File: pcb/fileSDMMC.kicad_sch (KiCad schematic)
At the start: 6 parts, among them J4 MicroSd

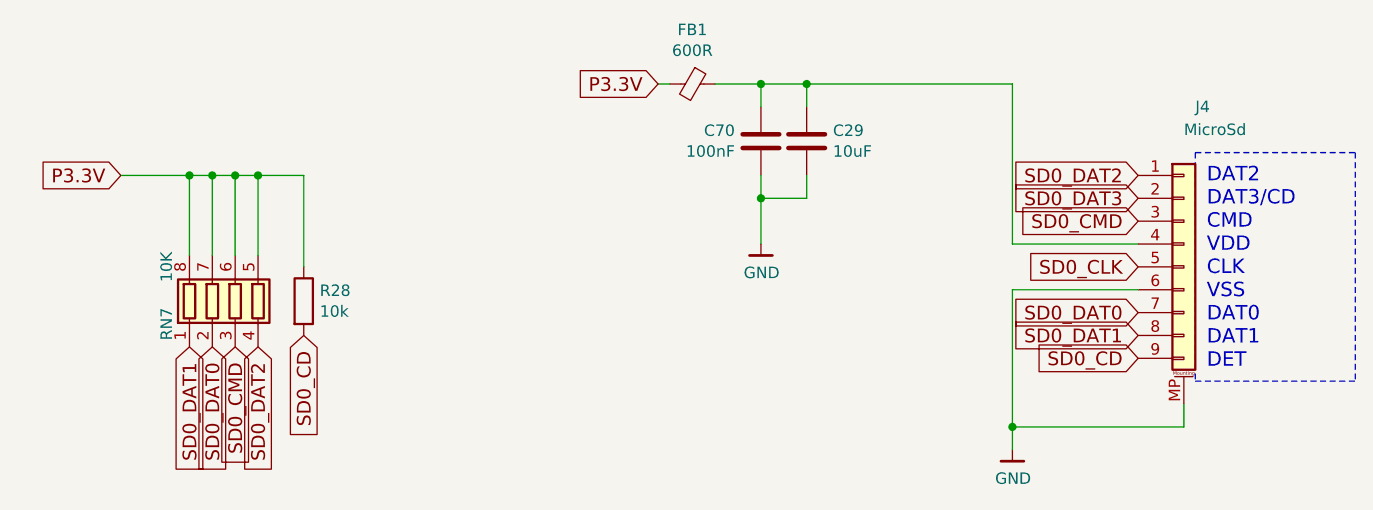
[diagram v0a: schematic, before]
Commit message: refactor(pcb): strip down
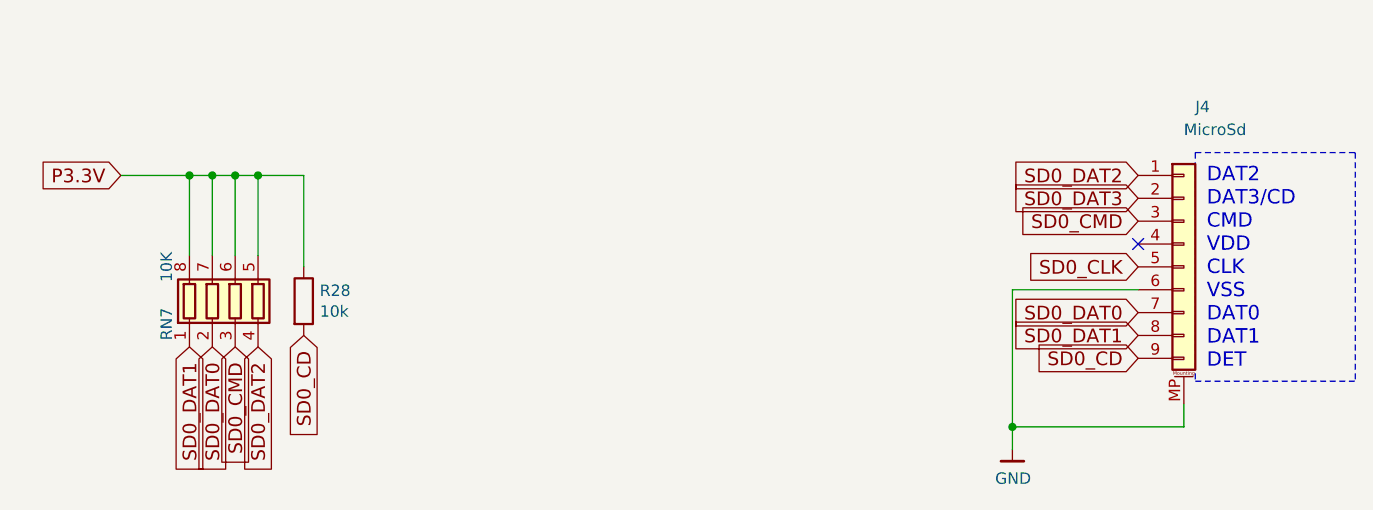
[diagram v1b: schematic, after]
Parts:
- removed C29: 10uF, Capacitor_SMD:C_0402_1005Metric, symbol Device:C
- removed C70: 100nF, Capacitor_SMD:C_0201_0603Metric, symbol Device:C
- removed FB1: 600R, Inductor_SMD:L_0402_1005Metric, symbol Device:Ferrite_Bead_Small
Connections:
- no-connect marks 0 -> 1
